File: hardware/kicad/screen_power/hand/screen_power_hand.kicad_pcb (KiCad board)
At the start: 2 copper layers, 68 x 76 mm, 48 parts, among them J1 AUX 5V INPUT, J101 PI USB / XH4, J102 TOUCH / XH4, J103 SCREEN 1 POWER, J2 GPIO17 / GND, J201 PI USB / XH4, J202 TOUCH / XH4, J203 SCREEN 2 POWER, K101 IM02TS, K201 IM02TS, Q1 2N3904, Q101 TN0702, Q2 2N3906, Q201 TN0702, Q3 SUP70101EL, Q4 SUP70101EL, U1 LMC7660IN, U2 TLP627M

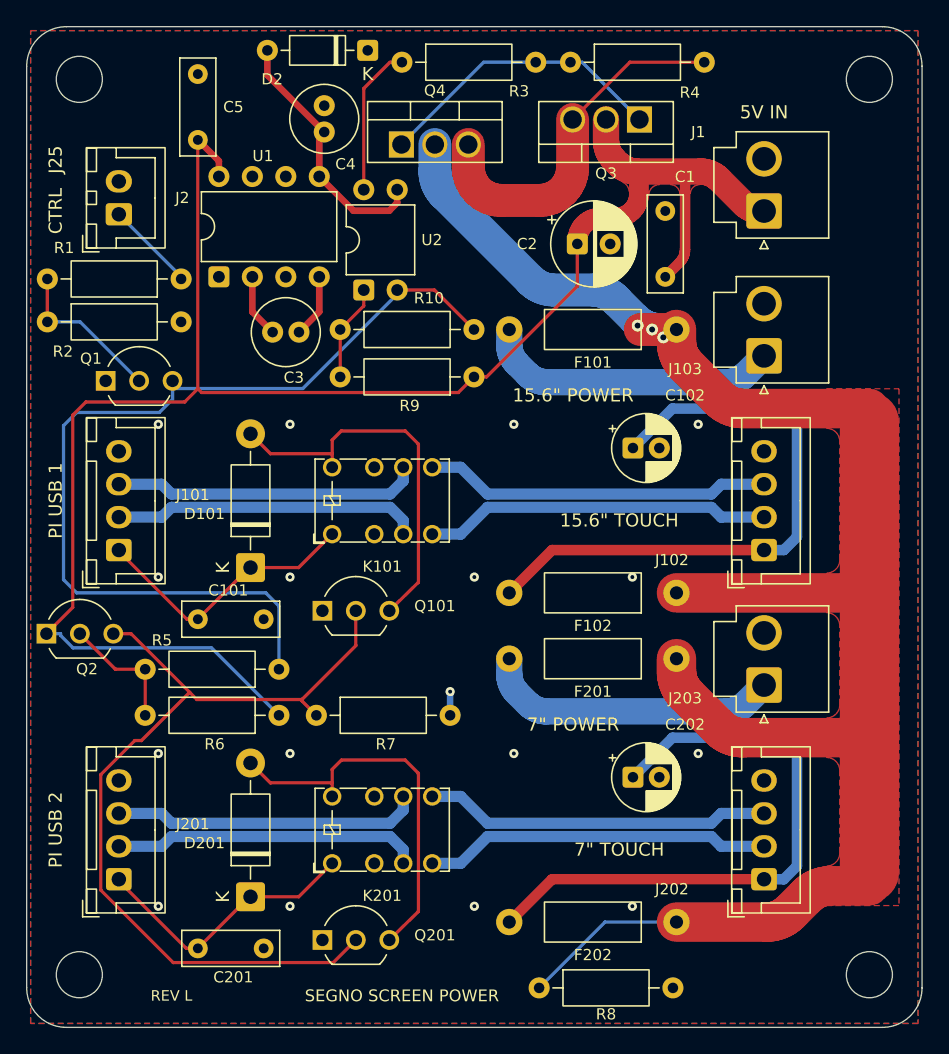
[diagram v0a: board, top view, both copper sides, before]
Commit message: fix(hardware): finish rounded routing across all three boards
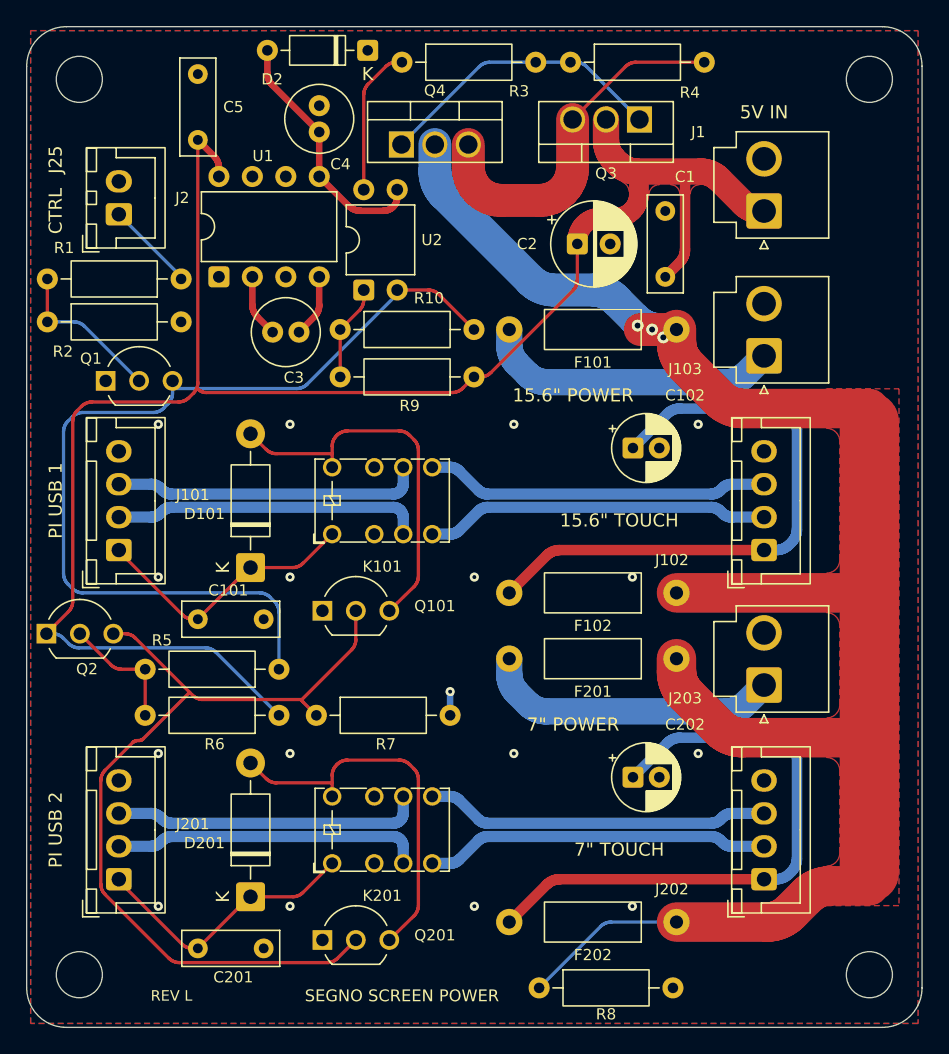
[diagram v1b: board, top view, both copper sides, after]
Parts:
- moved C4 0.38 mm to (22.2, 6.00)
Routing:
- net AUX_5V: track 139.1 -> 138.4 mm
- net NEG_5V: track 19.8 -> 19.3 mm

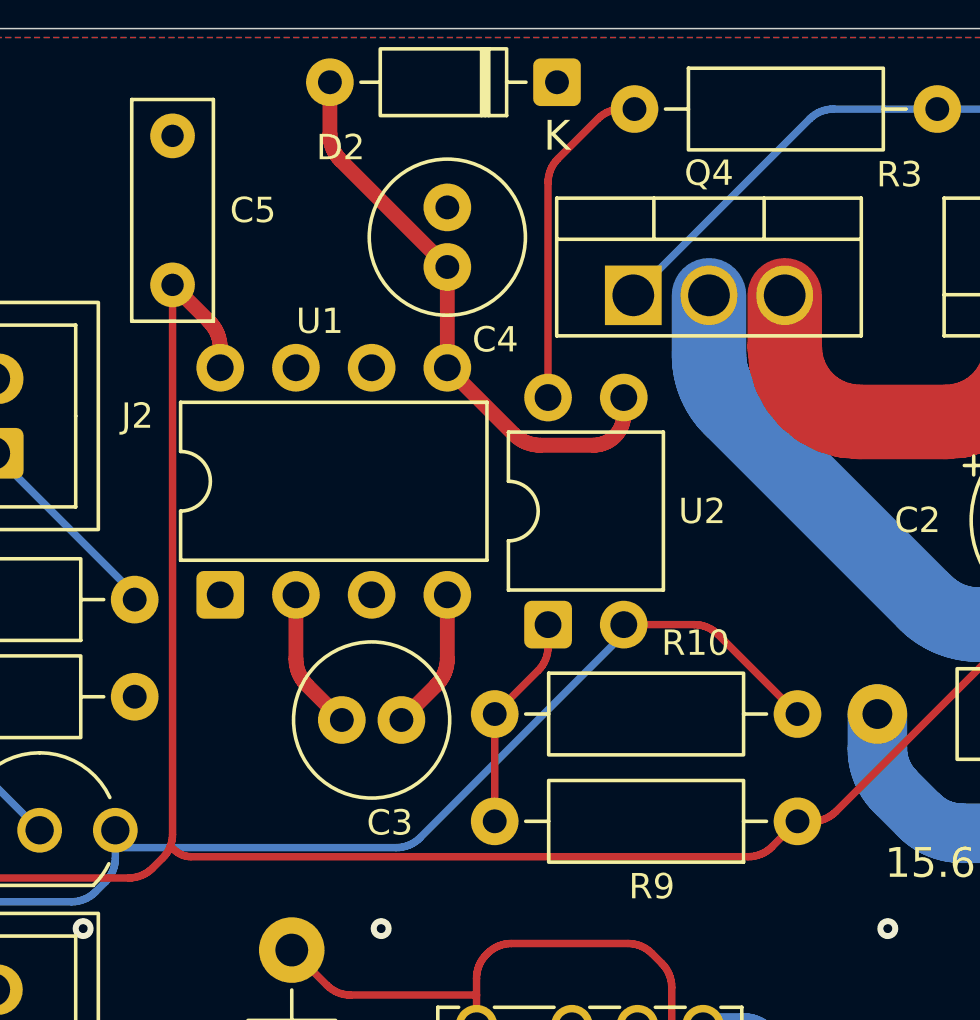
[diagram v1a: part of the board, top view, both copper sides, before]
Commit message: fix(hardware): align screen power ICs with clear courtyards
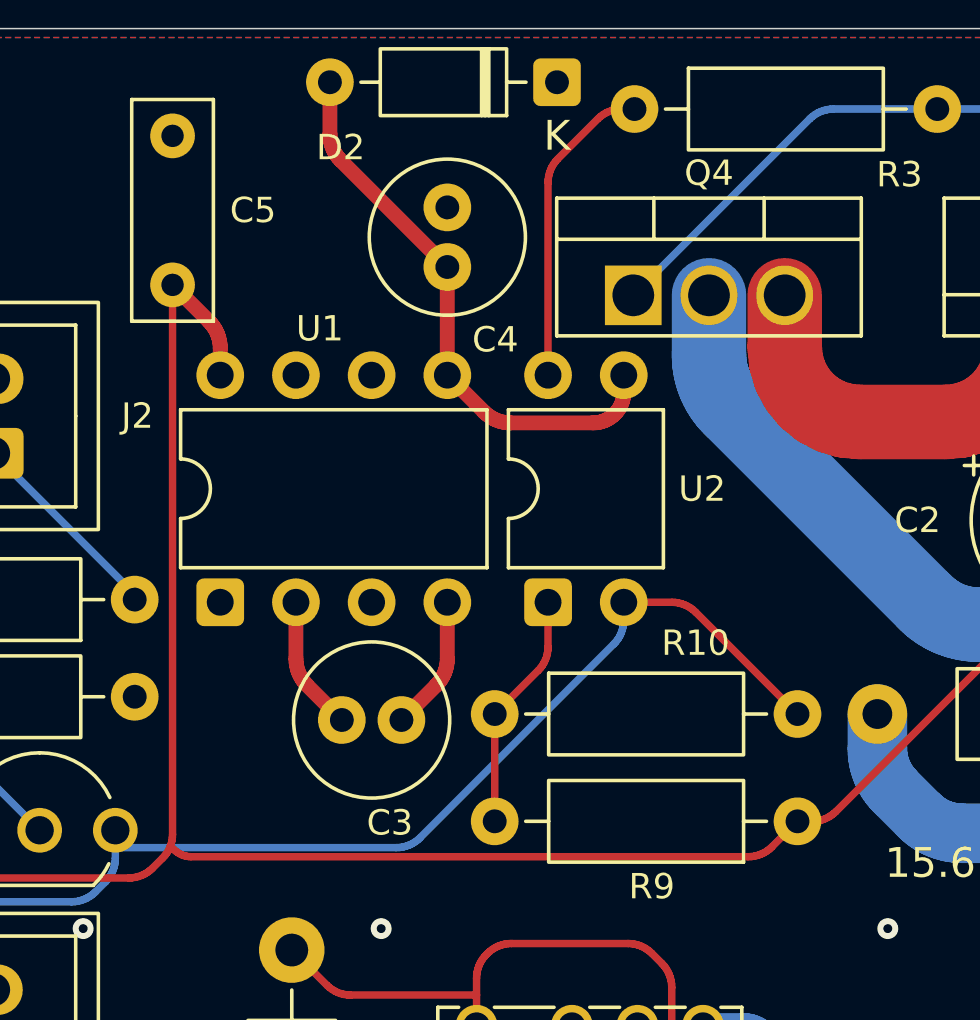
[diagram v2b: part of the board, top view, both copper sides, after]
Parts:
- moved U2 0.75 mm to (25.6, 19.2)
- moved U1 0.25 mm to (14.6, 19.2)
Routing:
- net CONTROL_SINK: track 71.1 -> 72.1 mm
- net GATE_SINK: track 11.3 -> 10.6 mm
- net GATE_LED: track 7.29 -> 8.04 mm
